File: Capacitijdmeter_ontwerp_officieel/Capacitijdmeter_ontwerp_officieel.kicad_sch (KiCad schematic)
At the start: 3 parts, among them U1 74HC14

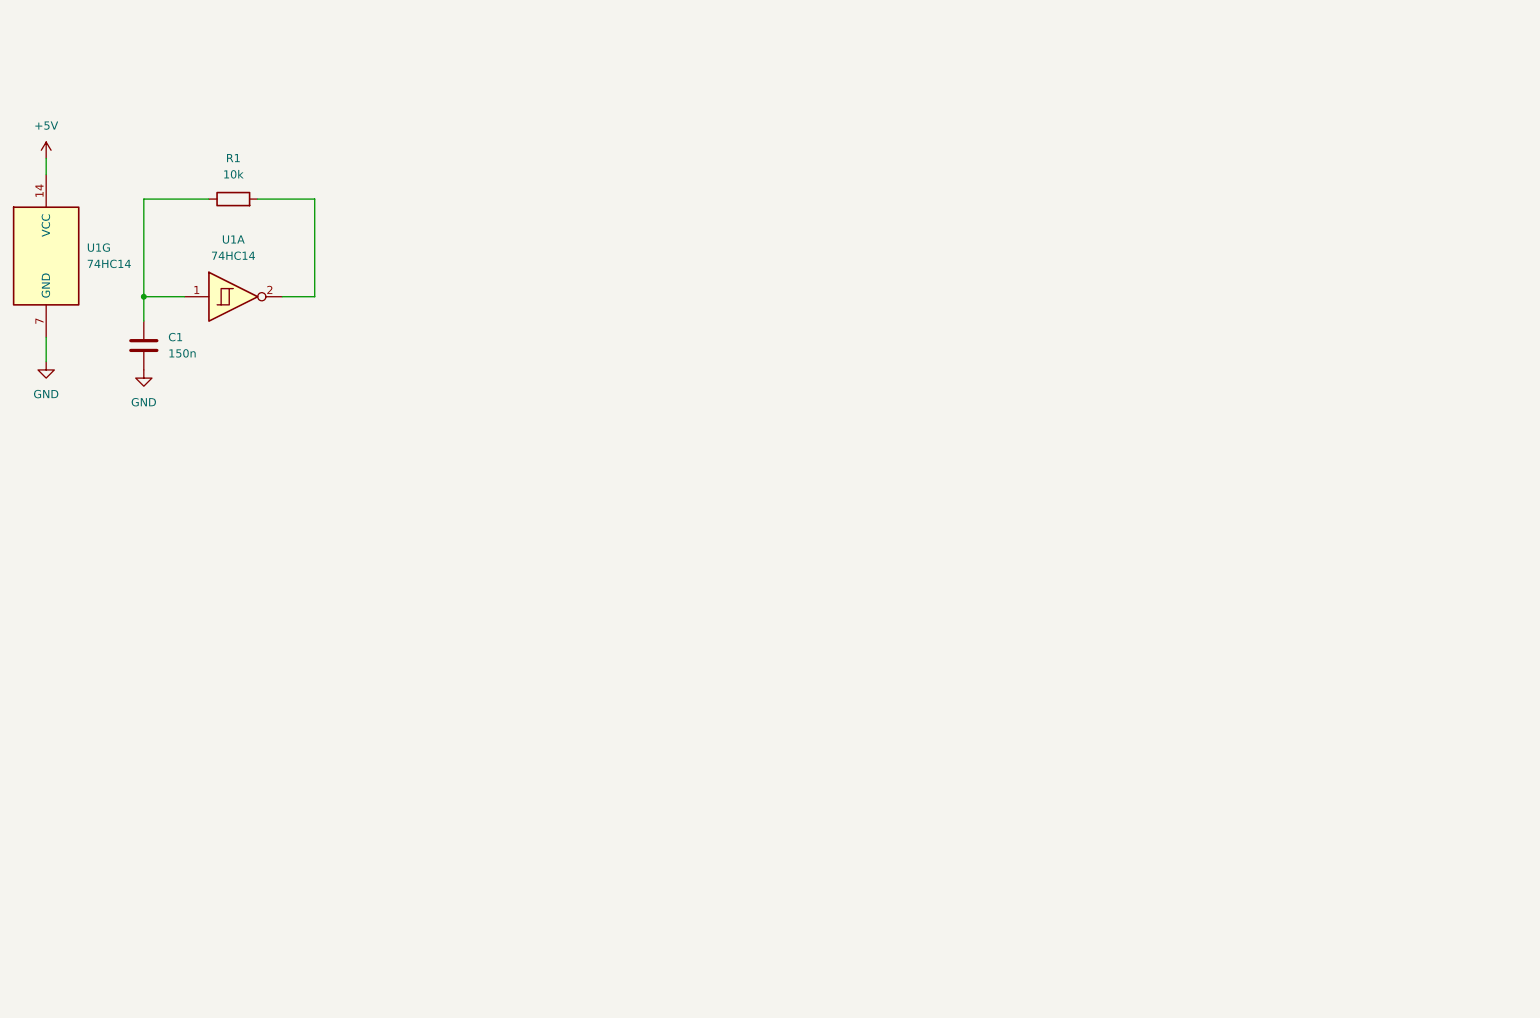
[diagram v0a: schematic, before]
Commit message: added 4 bit counter unit
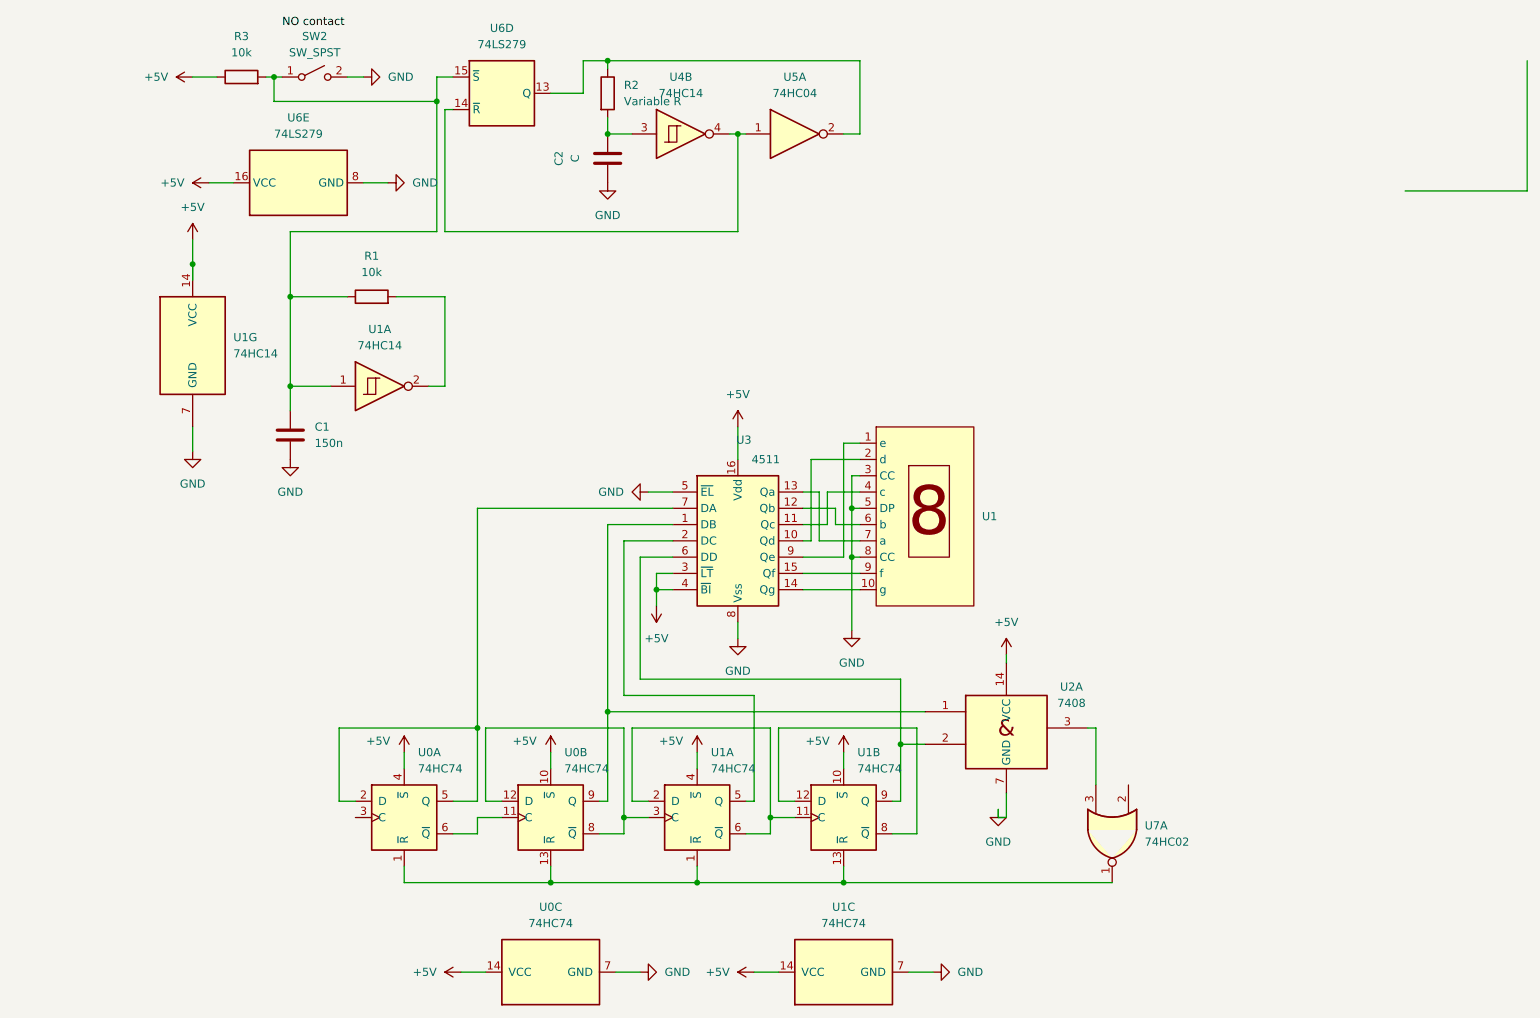
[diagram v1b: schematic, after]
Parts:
- added C2: C, symbol Device:C
- added R2: Variable R, symbol Device:R
- added R3: 10k, symbol Device:R
- added SW2: SW_SPST, symbol Switch:SW_SPST
- added U0, U1: 74HC74, symbol 74xx:74HC74
- added U1: (no value), symbol New_Library:CS56-11EWA
- added unit 3 of U1
- added unit 2 of U1
- added U2: 7408, symbol 74xx_IEEE:7408
- added U3: 4511, symbol 4xxx_IEEE:4511
- added U4: 74HC14, Package_DIP:DIP-14_W7.62mm_Socket_LongPads, symbol 74xx:74HC14
- added U5: 74HC04, symbol 74xx:74HC04
- added U6: 74LS279, symbol 74xx:74LS279
- added U7: 74HC02, symbol 74xx:74HC02
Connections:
- net +5V: now also R3.1, U0.10 (~{S}), U0.14 (VCC), U0.4 (~{S}), U1.10 (~{S}), U1.14 (VCC), U1.4 (~{S}), U2.14 (VCC), U3.16 (Vdd), U3.3 (~{LT}), U3.4 (~{BI}), U6.16 (VCC)
- net GND: now also C2.2, SW2.2 (B), U0.7 (GND), U1.3 (CC), U1.5 (DP), U1.7 (GND), U1.8 (CC), U2.7 (GND), U3.5 (~{EL}), U3.8 (Vss), U6.8 (GND)
- net at C1.1, R1.1, U1.1: now also R3.2, SW2.1 (A), U6.15 (~{S})
- new net: R2.1, U5.2, U6.13 (Q)
- new net: U4.4, U5.1, U6.14 (~{R})
- new net: U1.1 (e), U3.9 (Qe)
- new net: U1.10 (g), U3.14 (Qg)
- new net: U1.2 (d), U3.10 (Qd)
- new net: U1.4 (c), U3.11 (Qc)
- new net: U1.6 (b), U3.12 (Qb)
- new net: U1.7 (a), U3.13 (Qa)
- new net: U1.9 (f), U3.15 (Qf)
- new net: C2.1, R2.2, U4.3
- new net: U0.1 (~{R}), U0.13 (~{R}), U1.1 (~{R}), U1.13 (~{R}), U7.1
- new net: U2.3, U7.3
- new net: U0.9 (Q), U2.1, U3.1 (DB)
- new net: U1.9 (Q), U2.2, U3.6 (DD)
- new net: U1.5 (Q), U3.2 (DC)
- new net: U0.2 (D), U0.5 (Q), U3.7 (DA)
- new net: U0.11 (C), U0.6 (~{Q})
- new net: U1.11 (C), U1.2 (D), U1.6 (~{Q})
- new net: U1.12 (D), U1.8 (~{Q})
- new net: U0.12 (D), U0.8 (~{Q}), U1.3 (C)
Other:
- moved on the sheet: C1, R1, U1A, U1G

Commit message: fixes
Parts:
- removed R3: 10k, symbol Device:R
- removed U4: 74HC14, Package_DIP:DIP-14_W7.62mm_Socket_LongPads, symbol 74xx:74HC14
- removed U5: 74HC04, symbol 74xx:74HC04
- removed U6: 74LS279, symbol 74xx:74LS279
- added C3: C, symbol Device:C
- added J1: USB_A, symbol Connector:USB_A
- added R4: 10k, symbol Device:R
- added U10, U16, U22: 4511, symbol 4xxx_IEEE:4511
- added U11, U17, U23: (no value), symbol New_Library:CS56-11EWA
- added U12: 7408, Package_DIP:DIP-14_W7.62mm_Socket_LongPads, symbol 74xx_IEEE:7408
- added U14, U15, U20, U21, U8, U9: 74HC74, Package_DIP:DIP-14_W7.62mm_Socket_LongPads, symbol 74xx:74HC74
- added unit 3 of U2
- added unit 4 of U2
- added unit 2 of U2
- added U27, U28, U29: 74HC00, symbol 74xx:74HC00
- added unit 2 of U7
- added unit 5 of U7
- added unit 4 of U7
- added unit 3 of U7
- C2: value C -> Variable C
- U0, U1, U2: footprint (none) -> Package_DIP:DIP-14_W7.62mm_Socket_LongPads
- renumbered U1 to U26, U1 to U4
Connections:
- net +5V: now also C3.2, J1.1 (VBUS), R4.1, U10.16 (Vdd), U10.3 (~{LT}), U10.4 (~{BI}), U12.14 (VCC), U14.10 (~{S}), U14.14 (VCC), U14.4 (~{S}), U15.10 (~{S}), U15.14 (VCC), U15.4 (~{S}), U16.16 (Vdd), U16.3 (~{LT}), U16.4 (~{BI}), U2.14 (VCC), U2.14 (VCC), U2.14 (VCC), U20.10 (~{S}), U20.14 (VCC), U20.4 (~{S}), U21.10 (~{S}), U21.14 (VCC), U21.4 (~{S}), U22.16 (Vdd), U22.3 (~{LT}), U22.4 (~{BI}), U28.14 (VCC), U7.14 (VCC), U8.10 (~{S}), U8.14 (VCC), U8.4 (~{S}), U9.10 (~{S}), U9.14 (VCC), U9.4 (~{S})
- net GND: now also R2.2, C3.1, J1.4 (GND), J1.SH (Shield), U10.5 (~{EL}), U10.8 (Vss), U11.3 (CC), U11.5 (DP), U11.8 (CC), U12.7 (GND), U14.7 (GND), U15.7 (GND), U16.5 (~{EL}), U16.8 (Vss), U17.3 (CC), U17.5 (DP), U17.8 (CC), U2.7 (GND), U2.7 (GND), U2.7 (GND), U20.7 (GND), U21.7 (GND), U22.5 (~{EL}), U22.8 (Vss), U23.3 (CC), U23.5 (DP), U23.8 (CC), U28.7 (GND), U7.7 (GND), U8.7 (GND), U9.7 (GND); no longer C2.2
- net at R2.1: now also C2.2, U28.4, U28.5
- net at C1.1, R1.1, U4.1: no longer SW2.1 (A)
- net at C2.1: now also U27.3; no longer R2.2
- net at U7.2: now also U7.11, U7.5, U7.8
- net at R1.2, U4.2: now also U12.2
- net at U0.3 (C): now also U2.6, U7.6
- new net: U9.11 (C), U9.2 (D), U9.6 (~{Q})
- new net: U9.12 (D), U9.8 (~{Q})
- new net: U7.4, U8.1 (~{R}), U8.13 (~{R}), U9.1 (~{R}), U9.13 (~{R})
- new net: U10.6 (DD), U2.5, U9.9 (Q)
- new net: U15.9 (Q), U16.6 (DD), U2.10
- new net: U2.8, U7.9, U8.3 (C)
- new net: U14.9 (Q), U16.1 (DB), U2.9
- new net: U22.9 (Qe), U23.1 (e)
- new net: U22.14 (Qg), U23.10 (g)
- new net: U22.10 (Qd), U23.2 (d)
- new net: U22.11 (Qc), U23.4 (c)
- new net: U22.12 (Qb), U23.6 (b)
- new net: U22.13 (Qa), U23.7 (a)
- new net: U22.15 (Qf), U23.9 (f)
- new net: U16.10 (Qd), U17.2 (d)
- new net: U16.11 (Qc), U17.4 (c)
- new net: U16.12 (Qb), U17.6 (b)
- new net: U16.13 (Qa), U17.7 (a)
- new net: U16.14 (Qg), U17.10 (g)
- new net: U16.15 (Qf), U17.9 (f)
- new net: U15.5 (Q), U16.2 (DC)
- new net: U14.2 (D), U14.5 (Q), U16.7 (DA)
- new net: U16.9 (Qe), U17.1 (e)
- new net: U10.7 (DA), U8.2 (D), U8.5 (Q)
- new net: U8.11 (C), U8.6 (~{Q})
- new net: U14.3 (C), U2.11, U7.12
- new net: U2.12, U20.9 (Q), U22.1 (DB)
- new net: U2.13, U21.9 (Q), U22.6 (DD)
- new net: U10.9 (Qe), U11.1 (e)
- new net: U10.14 (Qg), U11.10 (g)
- new net: U10.10 (Qd), U11.2 (d)
- new net: U10.11 (Qc), U11.4 (c)
- new net: U10.12 (Qb), U11.6 (b)
- new net: U10.13 (Qa), U11.7 (a)
- new net: U10.15 (Qf), U11.9 (f)
- new net: U21.11 (C), U21.2 (D), U21.6 (~{Q})
- new net: U21.12 (D), U21.8 (~{Q})
- new net: U20.1 (~{R}), U20.13 (~{R}), U21.1 (~{R}), U21.13 (~{R}), U7.13
- new net: U10.1 (DB), U2.4, U8.9 (Q)
- new net: U27.1, U28.6, U29.10, U29.9
- new net: U12.1, U29.8
- new net: U8.12 (D), U8.8 (~{Q}), U9.3 (C)
- new net: U10.2 (DC), U9.5 (Q)
- new net: R4.2, SW2.1 (A), U27.2
- new net: U12.3, U20.3 (C)
- new net: U14.1 (~{R}), U14.13 (~{R}), U15.1 (~{R}), U15.13 (~{R}), U7.10
- new net: U15.11 (C), U15.2 (D), U15.6 (~{Q})
- new net: U14.12 (D), U14.8 (~{Q}), U15.3 (C)
- new net: U20.12 (D), U20.8 (~{Q}), U21.3 (C)
- new net: U21.5 (Q), U22.2 (DC)
- new net: U20.11 (C), U20.6 (~{Q})
- new net: U14.11 (C), U14.6 (~{Q})
- new net: U20.5 (Q), U22.7 (DA)
- new net: U15.12 (D), U15.8 (~{Q})
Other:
- moved on the sheet: C1, R1, R2, U0A, U0B, U0C, U1A, U1B, U1C, U26, U2A, U3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

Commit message: updat
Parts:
- removed J1: USB_A, symbol Connector:USB_A
- added C4: C, symbol Device:C
- added J2: USB_C_Receptacle_PowerOnly_6P, symbol Connector:USB_C_Receptacle_PowerOnly_6P
- added R3, R5: 5k1, symbol Device:R
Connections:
- net +5V: now also C3.1, J2.A9 (VBUS), J2.B9 (VBUS); no longer C3.2
- net GND: now also C3.2, C4.2, J2.A12 (GND), J2.B12 (GND), J2.SH (SHIELD), R3.1, R5.1; no longer C3.1
- net V_{e3}: now reaches U26.1 (e), U3.9 (Qe)
- net V_{g3}: now reaches U26.10 (g), U3.14 (Qg)
- net V_{d3}: now reaches U26.2 (d), U3.10 (Qd)
- net V_{c3}: now reaches U26.4 (c), U3.11 (Qc)
- net V_{b3}: now reaches U26.6 (b), U3.12 (Qb)
- net V_{a3}: now reaches U26.7 (a), U3.13 (Qa)
- net V_{f3}: now reaches U26.9 (f), U3.15 (Qf)
- net V_{clk1}: now reaches U2.8, U7.9, U8.3 (C)
- net V_{CounterMR}: now reaches U7.11, U7.2, U7.5, U7.8
- net V_{clk0}: now reaches U0.3 (C), U2.6, U7.6
- net at U14.5 (Q), U16.7 (DA): no longer U14.2 (D)
- net at U10.7 (DA), U8.5 (Q): no longer U8.2 (D)
- net at U8.11 (C), U8.6 (~{Q}): now also U8.2 (D)
- net V_{counteroverflow}: now reaches U2.3, U7.3
- net V_{clk2}: now reaches U14.3 (C), U2.11, U7.12
- net V_{oneshot}: now reaches U29.8
- net V_{oneshot}: now also U12.2; no longer U12.1
- net at R4.2, SW2.1 (A), U27.2: now also C4.1
- net at U0.5 (Q), U3.7 (DA): no longer U0.2 (D)
- net V_{oscillator}: now reaches R1.2, U4.2
- net V_{oscillator}: now also U12.1; no longer U12.2
- net at U20.11 (C), U20.6 (~{Q}): now also U20.2 (D)
- net at U0.11 (C), U0.6 (~{Q}): now also U0.2 (D)
- net at U14.11 (C), U14.6 (~{Q}): now also U14.2 (D)
- new net: J2.B5 (CC2), R3.2
- new net: J2.A5 (CC1), R5.2
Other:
- moved on the sheet: C1, C2, R1, R2, R4, SW2, U26, U27A, U28B, U28E, U29C, U4A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

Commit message: added some footprints
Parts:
- U0, U1, U12, U14, U15, U2, U20, U21, U4, U8, U9: footprint Package_DIP:DIP-14_W7.62mm_Socket_LongPads -> Package_SO:SOIC-14_3.9x8.7mm_P1.27mm
- U10, U16, U22, U27, U28, U29, U3, U7: footprint (none) -> Package_SO:SOIC-14_3.9x8.7mm_P1.27mm
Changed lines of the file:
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@@
 			)
 		)
-		(property "Footprint" "Package_DIP:DIP-14_W7.62mm_Socket_LongPads"
+		(property "Footprint" "Package_SO:SOIC-14_3.9x8.7mm_P1.27mm"
 			(at 233.68 176.53 0)
 			(hide yes)
@@
 			)
 		)
-		(property "Footprint" "Package_DIP:DIP-14_W7.62mm_Socket_LongPads"
+		(property "Footprint" "Package_SO:SOIC-14_3.9x8.7mm_P1.27mm"
 			(at 187.96 200.66 0)
 			(hide yes)
@@
 			)
 		)
-		(property "Footprint" "Package_DIP:DIP-14_W7.62mm_Socket_LongPads"
+		(property "Footprint" "Package_SO:SOIC-14_3.9x8.7mm_P1.27mm"
 			(at 457.2 200.66 0)
 			(hide yes)
@@
 			)
 		)
-		(property "Footprint" "Package_DIP:DIP-14_W7.62mm_Socket_LongPads"
+		(property "Footprint" "Package_SO:SOIC-14_3.9x8.7mm_P1.27mm"
 			(at 394.97 162.56 0)
 			(hide yes)
@@
 			)
 		)
-		(property "Footprint" ""
+		(property "Footprint" "Package_SO:SOIC-14_3.9x8.7mm_P1.27mm"
 			(at 275.59 179.07 0)
 			(hide yes)
@@
 			)
 		)
-		(property "Footprint" ""
+		(property "Footprint" "Package_SO:SOIC-14_3.9x8.7mm_P1.27mm"
 			(at 353.06 133.35 0)
 			(hide yes)
@@
 			)
 		)
-		(property "Footprint" "Package_DIP:DIP-14_W7.62mm_Socket_LongPads"
+		(property "Footprint" "Package_SO:SOIC-14_3.9x8.7mm_P1.27mm"
 			(at 54.61 200.66 0)
 			(hide yes)
@@
 			)
 		)
-		(property "Footprint" "Package_DIP:DIP-14_W7.62mm_Socket_LongPads"
+		(property "Footprint" "Package_SO:SOIC-14_3.9x8.7mm_P1.27mm"
 			(at 165.1 176.53 0)
 			(hide yes)
@@
 			)
 		)
-		(property "Footprint" ""
+		(property "Footprint" "Package_SO:SOIC-14_3.9x8.7mm_P1.27mm"
 			(at 142.24 179.07 0)
 			(hide yes)
@@
 			)
 		)
-		(property "Footprint" "Package_DIP:DIP-14_W7.62mm_Socket_LongPads"
+		(property "Footprint" "Package_SO:SOIC-14_3.9x8.7mm_P1.27mm"
 			(at 528.32 162.56 0)
 			(hide yes)
@@
 			)
 		)
-		(property "Footprint" "Package_DIP:DIP-14_W7.62mm_Socket_LongPads"
+		(property "Footprint" "Package_SO:SOIC-14_3.9x8.7mm_P1.27mm"
 			(at 502.92 176.53 0)
 			(hide yes)
@@
 			)
 		)
-		(property "Footprint" "Package_DIP:DIP-14_W7.62mm_Socket_LongPads"
+		(property "Footprint" "Package_SO:SOIC-14_3.9x8.7mm_P1.27mm"
 			(at 259.08 162.56 0)
 			(hide yes)
@@
 			)
 		)
-		(property "Footprint" ""
+		(property "Footprint" "Package_SO:SOIC-14_3.9x8.7mm_P1.27mm"
 			(at 86.36 53.34 0)
 			(hide yes)
@@
 			)
 		)
-		(property "Footprint" ""
+		(property "Footprint" "Package_SO:SOIC-14_3.9x8.7mm_P1.27mm"
 			(at 107.95 45.72 0)
 			(hide yes)
@@
 			)
 		)
-		(property "Footprint" "Package_DIP:DIP-14_W7.62mm_Socket_LongPads"
+		(property "Footprint" "Package_SO:SOIC-14_3.9x8.7mm_P1.27mm"
 			(at 210.82 176.53 0)
 			(hide yes)
@@
 			)
 		)
-		(property "Footprint" "Package_DIP:DIP-14_W7.62mm_Socket_LongPads"
+		(property "Footprint" "Package_SO:SOIC-14_3.9x8.7mm_P1.27mm"
 			(at 125.73 162.56 0)
 			(hide yes)
@@
 			)
 		)
-		(property "Footprint" "Package_DIP:DIP-14_W7.62mm_Socket_LongPads"
+		(property "Footprint" "Package_SO:SOIC-14_3.9x8.7mm_P1.27mm"
 			(at 233.68 200.66 0)
 			(hide yes)
@@
 			)
 		)
-		(property "Footprint" ""
+		(property "Footprint" "Package_SO:SOIC-14_3.9x8.7mm_P1.27mm"
 			(at 83.82 133.35 0)
 			(hide yes)
@@
 			)
 		)
-		(property "Footprint" "Package_DIP:DIP-14_W7.62mm_Socket_LongPads"
+		(property "Footprint" "Package_SO:SOIC-14_3.9x8.7mm_P1.27mm"
 			(at 100.33 200.66 0)
 			(hide yes)
@@
 			)
 		)
-		(property "Footprint" ""
+		(property "Footprint" "Package_SO:SOIC-14_3.9x8.7mm_P1.27mm"
 			(at 281.94 212.09 0)
 			(hide yes)
@@
 			)
 		)
-		(property "Footprint" "Package_DIP:DIP-14_W7.62mm_Socket_LongPads"
+		(property "Footprint" "Package_SO:SOIC-14_3.9x8.7mm_P1.27mm"
 			(at 181.61 54.61 0)
 			(hide yes)
@@
 			)
 		)
-		(property "Footprint" "Package_DIP:DIP-14_W7.62mm_Socket_LongPads"
+		(property "Footprint" "Package_SO:SOIC-14_3.9x8.7mm_P1.27mm"
 			(at 346.71 176.53 0)
 			(hide yes)
@@
 			)
 		)
-		(property "Footprint" "Package_DIP:DIP-14_W7.62mm_Socket_LongPads"
+		(property "Footprint" "Package_SO:SOIC-14_3.9x8.7mm_P1.27mm"
 			(at 187.96 176.53 0)
 			(hide yes)
@@
 			)
 		)
-		(property "Footprint" "Package_DIP:DIP-14_W7.62mm_Socket_LongPads"
+		(property "Footprint" "Package_SO:SOIC-14_3.9x8.7mm_P1.27mm"
 			(at 369.57 200.66 0)
 			(hide yes)
@@
 			)
 		)
-		(property "Footprint" "Package_DIP:DIP-14_W7.62mm_Socket_LongPads"
+		(property "Footprint" "Package_SO:SOIC-14_3.9x8.7mm_P1.27mm"
 			(at 502.92 200.66 0)
 			(hide yes)
@@
 			)
 		)
-		(property "Footprint" "Package_DIP:DIP-14_W7.62mm_Socket_LongPads"
+		(property "Footprint" "Package_SO:SOIC-14_3.9x8.7mm_P1.27mm"
 			(at 480.06 176.53 0)
 			(hide yes)
@@
 			)
 		)
-		(property "Footprint" ""
+		(property "Footprint" "Package_SO:SOIC-14_3.9x8.7mm_P1.27mm"
 			(at 544.83 179.07 0)
 			(hide yes)
@@
 			)
 		)
-		(property "Footprint" ""
+		(property "Footprint" "Package_SO:SOIC-14_3.9x8.7mm_P1.27mm"
 			(at 217.17 133.35 0)
 			(hide yes)
@@
 			)
 		)
-		(property "Footprint" "Package_DIP:DIP-14_W7.62mm_Socket_LongPads"
+		(property "Footprint" "Package_SO:SOIC-14_3.9x8.7mm_P1.27mm"
 			(at 323.85 200.66 0)
 			(hide yes)
@@
 			)
 		)
-		(property "Footprint" ""
+		(property "Footprint" "Package_SO:SOIC-14_3.9x8.7mm_P1.27mm"
 			(at 66.04 31.75 0)
 			(hide yes)
@@
 			)
 		)
-		(property "Footprint" "Package_DIP:DIP-14_W7.62mm_Socket_LongPads"
+		(property "Footprint" "Package_SO:SOIC-14_3.9x8.7mm_P1.27mm"
 			(at 457.2 176.53 0)
 			(hide yes)
@@
 			)
 		)
-		(property "Footprint" "Package_DIP:DIP-14_W7.62mm_Socket_LongPads"
+		(property "Footprint" "Package_SO:SOIC-14_3.9x8.7mm_P1.27mm"
 			(at 165.1 40.64 0)
 			(hide yes)
@@
 			)
 		)
-		(property "Footprint" "Package_DIP:DIP-14_W7.62mm_Socket_LongPads"
+		(property "Footprint" "Package_SO:SOIC-14_3.9x8.7mm_P1.27mm"
 			(at 31.75 176.53 0)
 			(hide yes)
@@
 			)
 		)
-		(property "Footprint" "Package_DIP:DIP-14_W7.62mm_Socket_LongPads"
+		(property "Footprint" "Package_SO:SOIC-14_3.9x8.7mm_P1.27mm"
 			(at 300.99 176.53 0)
 			(hide yes)
@@
 			)
 		)
-		(property "Footprint" "Package_DIP:DIP-14_W7.62mm_Socket_LongPads"
+		(property "Footprint" "Package_SO:SOIC-14_3.9x8.7mm_P1.27mm"
 			(at 100.33 176.53 0)
 			(hide yes)
@@
 			)
 		)
-		(property "Footprint" ""
+		(property "Footprint" "Package_SO:SOIC-14_3.9x8.7mm_P1.27mm"
 			(at 486.41 133.35 0)
 			(hide yes)
@@
 			)
 		)
-		(property "Footprint" ""
+		(property "Footprint" "Package_SO:SOIC-14_3.9x8.7mm_P1.27mm"
 			(at 45.72 53.34 0)
 			(hide yes)
@@
 			)
 		)
-		(property "Footprint" "Package_DIP:DIP-14_W7.62mm_Socket_LongPads"
+		(property "Footprint" "Package_SO:SOIC-14_3.9x8.7mm_P1.27mm"
 			(at 369.57 176.53 0)
 			(hide yes)
@@
 			)
 		)
-		(property "Footprint" "Package_DIP:DIP-14_W7.62mm_Socket_LongPads"
+		(property "Footprint" "Package_SO:SOIC-14_3.9x8.7mm_P1.27mm"
 			(at 54.61 176.53 0)
 			(hide yes)
@@
 			)
 		)
-		(property "Footprint" "Package_DIP:DIP-14_W7.62mm_Socket_LongPads"
+		(property "Footprint" "Package_SO:SOIC-14_3.9x8.7mm_P1.27mm"
 			(at 323.85 176.53 0)
 			(hide yes)
@@
 			)
 		)
-		(property "Footprint" ""
+		(property "Footprint" "Package_SO:SOIC-14_3.9x8.7mm_P1.27mm"
 			(at 411.48 179.07 0)
 			(hide yes)
@@
 			)
 		)
-		(property "Footprint" "Package_DIP:DIP-14_W7.62mm_Socket_LongPads"
+		(property "Footprint" "Package_SO:SOIC-14_3.9x8.7mm_P1.27mm"
 			(at 434.34 176.53 0)
 			(hide yes)
@@
 			)
 		)
-		(property "Footprint" "Package_DIP:DIP-14_W7.62mm_Socket_LongPads"
+		(property "Footprint" "Package_SO:SOIC-14_3.9x8.7mm_P1.27mm"
 			(at 420.37 139.7 0)
 			(hide yes)
@@
 			)
 		)
-		(property "Footprint" "Package_DIP:DIP-14_W7.62mm_Socket_LongPads"
+		(property "Footprint" "Package_SO:SOIC-14_3.9x8.7mm_P1.27mm"
 			(at 77.47 176.53 0)
 			(hide yes)
